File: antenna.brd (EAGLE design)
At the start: 95 x 95 mm, 23 parts, among them X1 BU-SMA-V

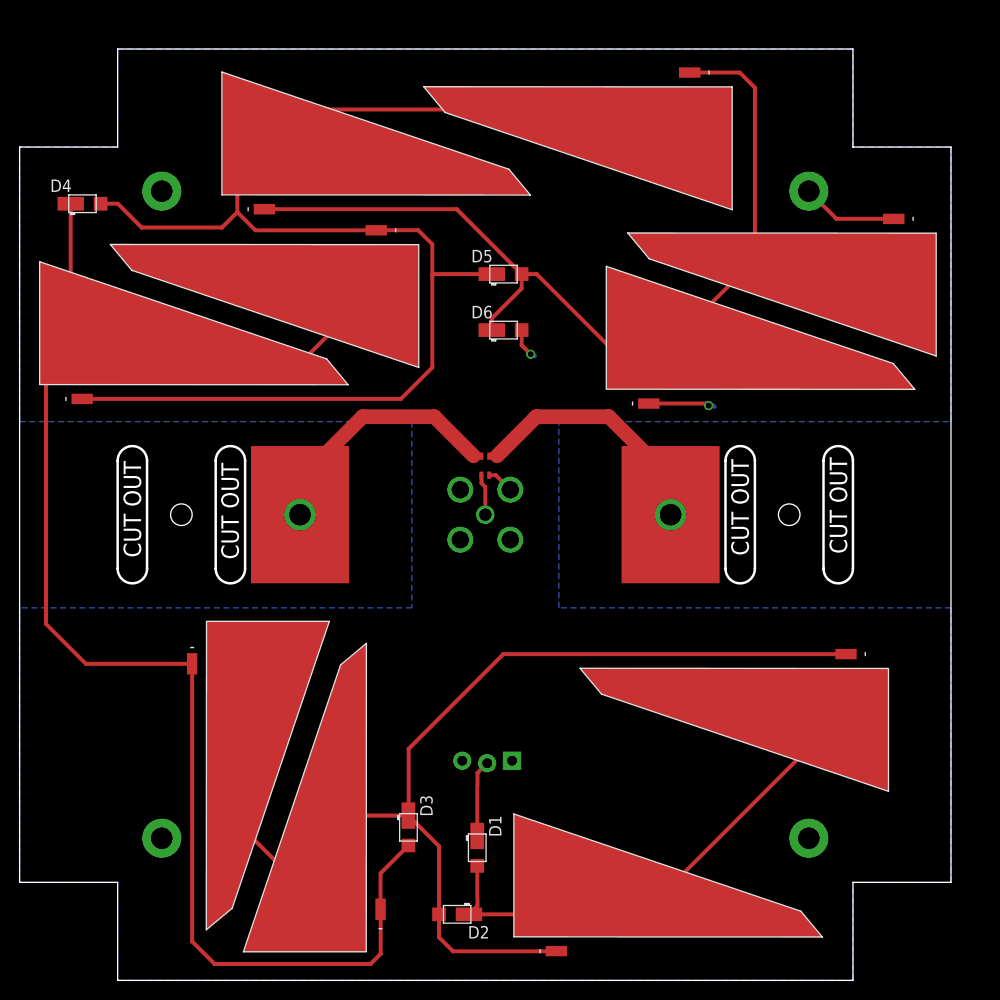
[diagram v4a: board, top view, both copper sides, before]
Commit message: Changed antenna board to accommodate pumpkin clips
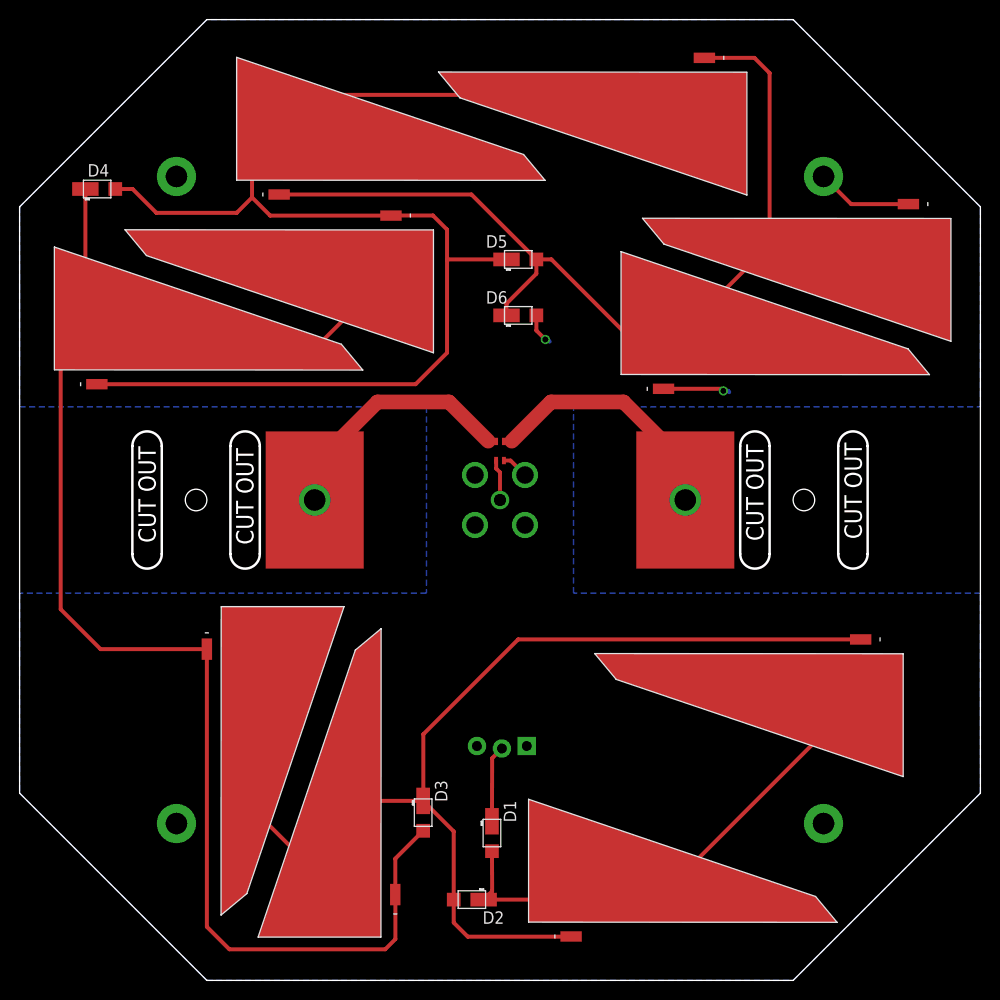
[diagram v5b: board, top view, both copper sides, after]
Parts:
- moved FRAME1 22.1 mm to (0.00, 0.00)
- moved B1 2.12 mm to (49.0, 54.0)
- moved D1 2.12 mm to (48.2, 15.0)
- moved D2 2.12 mm to (46.1, 8.24)
- moved D3 2.12 mm to (41.2, 17.1)
- moved D4 2.12 mm to (7.91, 80.7)
- moved D5 2.12 mm to (50.9, 73.5)
- moved D6 2.12 mm to (50.9, 67.8)
- moved JP1 2.12 mm to (51.7, 23.8)
- moved SL1 2.12 mm to (59.2, 6.07)
- moved SL10 2.12 mm to (68.7, 61.9)
- moved SL3 2.12 mm to (36.7, 11.8)
- moved SL4 2.12 mm to (20.7, 30.8)
- moved SL5 2.12 mm to (34.9, 76.4)
- moved SL6 2.12 mm to (10.9, 62.4)
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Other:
- board size 95 x 95 mm -> 98 x 98 mm
